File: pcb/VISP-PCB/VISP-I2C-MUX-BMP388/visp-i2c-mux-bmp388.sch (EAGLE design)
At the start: 37 parts, among them U1 MIC5225-3.3, U2 TCA9546APWR, U3 24C01ASM, U5 BMP388, U6 BMP388, U7 BMP388, U8 BMP388

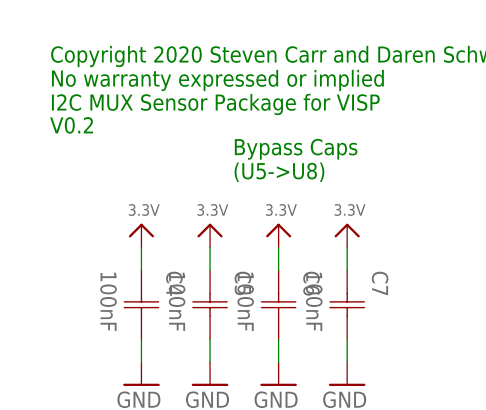
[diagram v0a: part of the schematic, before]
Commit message: Update notes in schematics for VISP PCB's
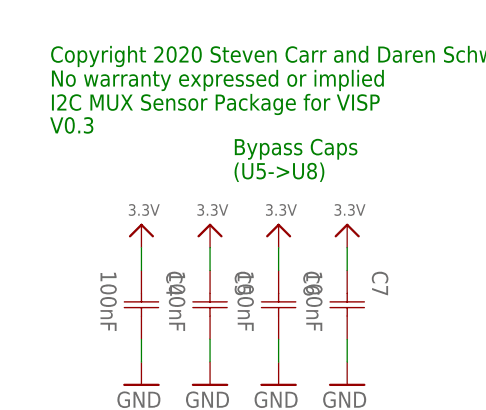
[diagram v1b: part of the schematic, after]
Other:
- note added: "V0.3"
- note removed: "V0.2"
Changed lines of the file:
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@@
 I2C MUX Sensor Package for VISP</text>
 <text x="68.58" y="144.78" size="1.778" layer="91">EEPROM to store Calibration Data</text>
-<text x="5.08" y="134.62" size="1.778" layer="91">V0.2</text>
+<text x="5.08" y="134.62" size="1.778" layer="91">V0.3</text>
 <text x="15.24" y="71.12" size="1.778" layer="91">Make U1 optional</text>
 <text x="114.3" y="-35.56" size="1.778" layer="97">For SPI set CSB low at startup
